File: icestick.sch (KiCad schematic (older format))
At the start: 2 parts, among them J1 Conn_01x10, J3 Conn_01x10

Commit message: Assigned footprints
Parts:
- J1, J3: footprint (none) -> Connector_PinHeader_2.54mm:PinHeader_1x10_P2.54mm_Vertical
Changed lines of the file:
@@
 F 0 "J1" H 2900 3700 50  0000 C CNN
 F 1 "Conn_01x10" H 2850 2500 50  0001 C CNN
-F 2 "" H 2900 3150 50  0001 C CNN
+F 2 "Connector_PinHeader_2.54mm:PinHeader_1x10_P2.54mm_Vertical" H 2900 3150 50  0001 C CNN
 F 3 "~" H 2900 3150 50  0001 C CNN
 	1    2900 3150
@@
 F 0 "J3" H 5720 3675 50  0000 C CNN
 F 1 "Conn_01x10" H 5720 3676 50  0001 C CNN
-F 2 "" H 5800 3150 50  0001 C CNN
+F 2 "Connector_PinHeader_2.54mm:PinHeader_1x10_P2.54mm_Vertical" H 5800 3150 50  0001 C CNN
 F 3 "~" H 5800 3150 50  0001 C CNN
 	1    5800 3150

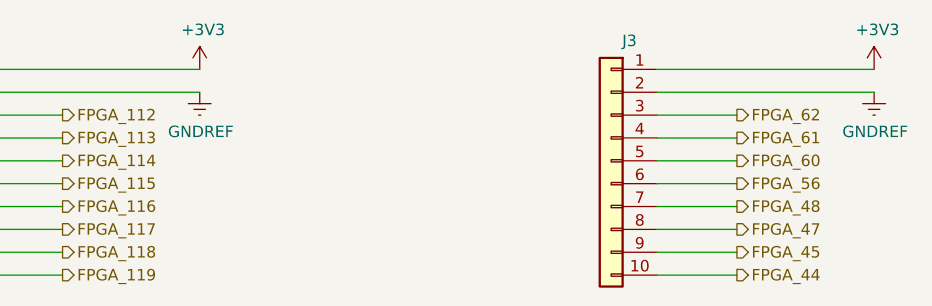
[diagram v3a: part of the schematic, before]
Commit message: Continued layouting
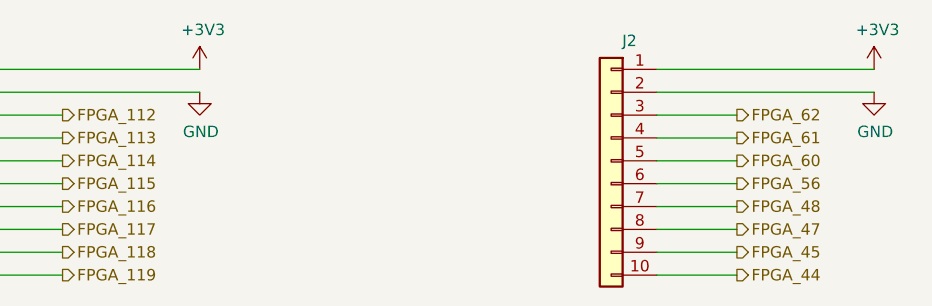
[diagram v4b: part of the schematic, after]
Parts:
- renumbered J3 to J2
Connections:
- net GNDREF renamed GND
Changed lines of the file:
@@
 $EndComp
 $Comp
-L power:+3V3 #PWR0101
+L power:+3V3 #PWR01
 U 1 1 5BCC5C29
 P 4000 2750
-F 0 "#PWR0101" H 4000 2600 50  0001 C CNN
+F 0 "#PWR01" H 4000 2600 50  0001 C CNN
 F 1 "+3V3" H 4015 2923 50  0000 C CNN
 F 2 "" H 4000 2750 50  0001 C CNN
@@
 Wire Wire Line
 	3100 2850 4000 2850
-$Comp
-L power:GNDREF #PWR0102
-U 1 1 5BCC6126
-P 4000 2850
-F 0 "#PWR0102" H 4000 2600 50  0001 C CNN
-F 1 "GNDREF" H 4005 2677 50  0000 C CNN
-F 2 "" H 4000 2850 50  0001 C CNN
-F 3 "" H 4000 2850 50  0001 C CNN
-	1    4000 2850
-	1    0    0    -1
-$EndComp
 Wire Wire Line
 	4000 2750 3100 2750
 $Comp
-L Connector_Generic:Conn_01x10 J3
+L Connector_Generic:Conn_01x10 J2
 U 1 1 5BCC6CE9
 P 5800 3150
-F 0 "J3" H 5720 3675 50  0000 C CNN
+F 0 "J2" H 5720 3675 50  0000 C CNN
 F 1 "Conn_01x10" H 5720 3676 50  0001 C CNN
 F 2 "Connector_PinHeader_2.54mm:PinHeader_1x10_P2.54mm_Vertical" H 5800 3150 50  0001 C CNN
@@
 $EndComp
 $Comp
-L power:+3V3 #PWR0103
+L power:+3V3 #PWR03
 U 1 1 5BCC6E8C
 P 6950 2750
-F 0 "#PWR0103" H 6950 2600 50  0001 C CNN
+F 0 "#PWR03" H 6950 2600 50  0001 C CNN
 F 1 "+3V3" H 6965 2923 50  0000 C CNN
 F 2 "" H 6950 2750 50  0001 C CNN
 F 3 "" H 6950 2750 50  0001 C CNN
 	1    6950 2750
-	1    0    0    -1
-$EndComp
-$Comp
-L power:GNDREF #PWR0104
-U 1 1 5BCC6E9B
-P 6950 2850
-F 0 "#PWR0104" H 6950 2600 50  0001 C CNN
-F 1 "GNDREF" H 6955 2677 50  0000 C CNN
-F 2 "" H 6950 2850 50  0001 C CNN
-F 3 "" H 6950 2850 50  0001 C CNN
-	1    6950 2850
 	1    0    0    -1
 $EndComp
@@
 Wire Wire Line
 	6000 3650 6350 3650
+$Comp
+L power:GND #PWR04
+U 1 1 5BCF7627
+P 6950 2850
+F 0 "#PWR04" H 6950 2600 50  0001 C CNN
+F 1 "GND" H 6955 2677 50  0000 C CNN
+F 2 "" H 6950 2850 50  0001 C CNN
+F 3 "" H 6950 2850 50  0001 C CNN
+	1    6950 2850
+	1    0    0    -1
+$EndComp
+$Comp
+L power:GND #PWR02
+U 1 1 5BCF767D
+P 4000 2850
+F 0 "#PWR02" H 4000 2600 50  0001 C CNN
+F 1 "GND" H 4005 2677 50  0000 C CNN
+F 2 "" H 4000 2850 50  0001 C CNN
+F 3 "" H 4000 2850 50  0001 C CNN
+	1    4000 2850
+	1    0    0    -1
+$EndComp
 $EndSCHEMATC

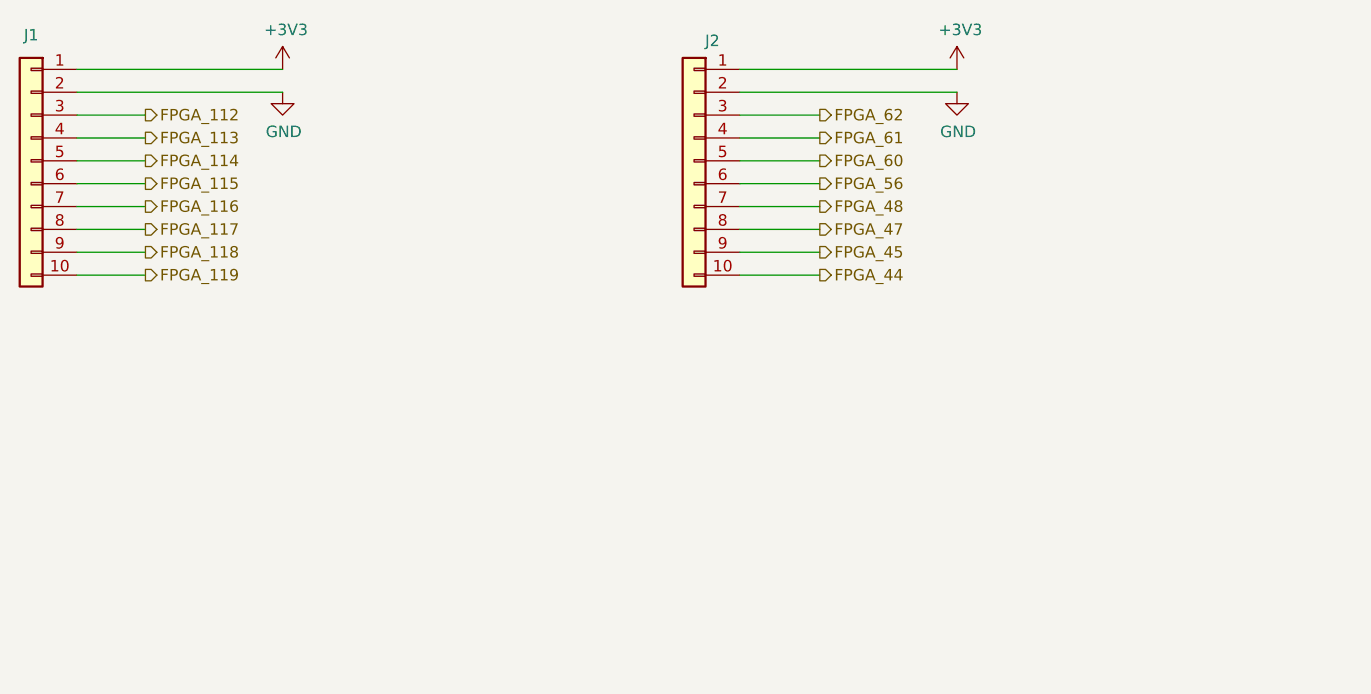
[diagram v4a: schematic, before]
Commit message: Began redesigning with Si8660
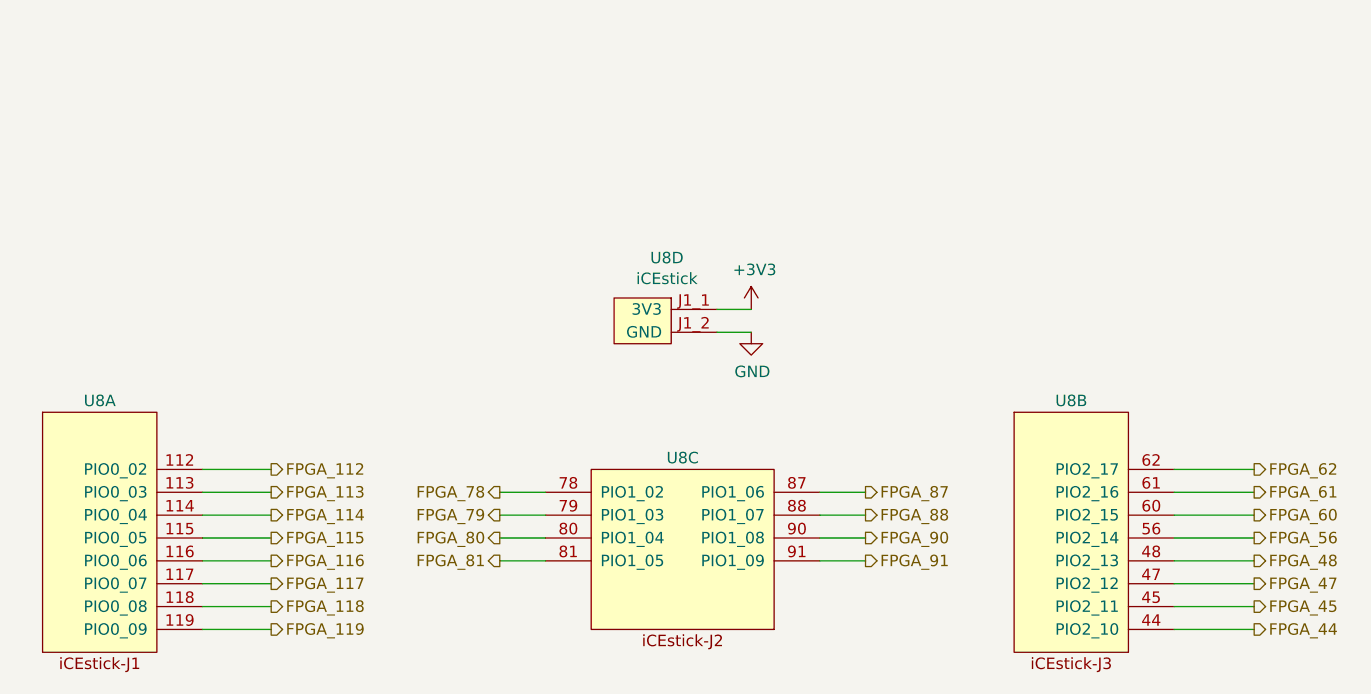
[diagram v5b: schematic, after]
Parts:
- removed J1, J2: Conn_01x10, Connector_PinHeader_2.54mm:PinHeader_1x10_P2.54mm_Vertical, symbol Connector_Generic:Conn_01x10
- added U8: iCEstick, Matthias:iCEstick, symbol Matthias:iCEstick
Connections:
- net +3V3: now also U8.J1_1 (3V3), U8.J2_12 (3V3), U8.J2_6 (3V3), U8.J3_1 (3V3)
- net FPGA_112: now also U8.112 (PIO0_02)
- net FPGA_113: now also U8.113 (PIO0_03)
- net FPGA_114: now also U8.114 (PIO0_04)
- net FPGA_115: now also U8.115 (PIO0_05)
- net FPGA_116: now also U8.116 (PIO0_06)
- net FPGA_117: now also U8.117 (PIO0_07)
- net FPGA_118: now also U8.118 (PIO0_08)
- net FPGA_119: now also U8.119 (PIO0_09)
- net FPGA_44: now also U8.44 (PIO2_10)
- net FPGA_45: now also U8.45 (PIO2_11)
- net FPGA_47: now also U8.47 (PIO2_12)
- net FPGA_48: now also U8.48 (PIO2_13)
- net FPGA_56: now also U8.56 (PIO2_14)
- net FPGA_60: now also U8.60 (PIO2_15)
- net FPGA_61: now also U8.61 (PIO2_16)
- net FPGA_62: now also U8.62 (PIO2_17)
- net GND: now also U8.J1_2 (GND), U8.J2_11 (GND), U8.J2_5 (GND), U8.J3_2 (GND)
- new net FPGA_78: U8.78 (PIO1_02)
- new net FPGA_79: U8.79 (PIO1_03)
- new net FPGA_80: U8.80 (PIO1_04)
- new net FPGA_81: U8.81 (PIO1_05)
- new net FPGA_87: U8.87 (PIO1_06)
- new net FPGA_88: U8.88 (PIO1_07)
- new net FPGA_90: U8.90 (PIO1_08)
- new net FPGA_91: U8.91 (PIO1_09)
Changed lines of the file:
@@
 $Descr A4 11693 8268
 encoding utf-8
-Sheet 2 11
+Sheet 11 11
 Title ""
 Date ""
@@
 Comment4 ""
 $EndDescr
-$Comp
-L Connector_Generic:Conn_01x10 J1
-U 1 1 5BCC5ADF
-P 2900 3150
-F 0 "J1" H 2900 3700 50  0000 C CNN
-F 1 "Conn_01x10" H 2850 2500 50  0001 C CNN
-F 2 "Connector_PinHeader_2.54mm:PinHeader_1x10_P2.54mm_Vertical" H 2900 3150 50  0001 C CNN
-F 3 "~" H 2900 3150 50  0001 C CNN
-	1    2900 3150
-	-1   0    0    -1
-$EndComp
-$Comp
-L power:+3V3 #PWR01
-U 1 1 5BCC5C29
-P 4000 2750
-F 0 "#PWR01" H 4000 2600 50  0001 C CNN
-F 1 "+3V3" H 4015 2923 50  0000 C CNN
-F 2 "" H 4000 2750 50  0001 C CNN
-F 3 "" H 4000 2750 50  0001 C CNN
-	1    4000 2750
-	1    0    0    -1
-$EndComp
-Text HLabel 3400 2950 2    50   Output ~ 0
+Text HLabel 3950 4500 2    50   Output ~ 0
 FPGA_112
-Text HLabel 3400 3050 2    50   Output ~ 0
+Text HLabel 3950 4600 2    50   Output ~ 0
 FPGA_113
-Text HLabel 3400 3150 2    50   Output ~ 0
+Text HLabel 3950 4700 2    50   Output ~ 0
 FPGA_114
-Text HLabel 3400 3250 2    50   Output ~ 0
+Text HLabel 3950 4800 2    50   Output ~ 0
 FPGA_115
-Text HLabel 3400 3350 2    50   Output ~ 0
+Text HLabel 3950 4900 2    50   Output ~ 0
 FPGA_116
-Text HLabel 3400 3450 2    50   Output ~ 0
+Text HLabel 3950 5000 2    50   Output ~ 0
 FPGA_117
-Text HLabel 3400 3550 2    50   Output ~ 0
+Text HLabel 3950 5100 2    50   Output ~ 0
 FPGA_118
-Text HLabel 3400 3650 2    50   Output ~ 0
+Text HLabel 3950 5200 2    50   Output ~ 0
 FPGA_119
 Wire Wire Line
-	3400 3650 3100 3650
+	3950 5200 3650 5200
 Wire Wire Line
-	3100 3550 3400 3550
+	3650 5100 3950 5100
 Wire Wire Line
-	3400 3450 3100 3450
+	3950 5000 3650 5000
 Wire Wire Line
-	3100 3350 3400 3350
+	3650 4900 3950 4900
 Wire Wire Line
-	3100 3250 3400 3250
+	3650 4800 3950 4800
 Wire Wire Line
-	3100 3150 3400 3150
+	3650 4700 3950 4700
 Wire Wire Line
-	3100 3050 3400 3050
+	3650 4600 3950 4600
 Wire Wire Line
-	3100 2950 3400 2950
-Wire Wire Line
-	3100 2850 4000 2850
-Wire Wire Line
-	4000 2750 3100 2750
+	3650 4500 3950 4500
 $Comp
-L Connector_Generic:Conn_01x10 J2
-U 1 1 5BCC6CE9
-P 5800 3150
-F 0 "J2" H 5720 3675 50  0000 C CNN
-F 1 "Conn_01x10" H 5720 3676 50  0001 C CNN
-F 2 "Connector_PinHeader_2.54mm:PinHeader_1x10_P2.54mm_Vertical" H 5800 3150 50  0001 C CNN
-F 3 "~" H 5800 3150 50  0001 C CNN
-	1    5800 3150
-	-1   0    0    -1
-$EndComp
-$Comp
-L power:+3V3 #PWR03
+L power:+3V3 #PWR056
 U 1 1 5BCC6E8C
-P 6950 2750
-F 0 "#PWR03" H 6950 2600 50  0001 C CNN
-F 1 "+3V3" H 6965 2923 50  0000 C CNN
-F 2 "" H 6950 2750 50  0001 C CNN
-F 3 "" H 6950 2750 50  0001 C CNN
-	1    6950 2750
+P 6050 3800
+F 0 "#PWR056" H 6050 3650 50  0001 C CNN
+F 1 "+3V3" H 6065 3973 50  0000 C CNN
+F 2 "" H 6050 3800 50  0001 C CNN
+F 3 "" H 6050 3800 50  0001 C CNN
+	1    6050 3800
 	1    0    0    -1
 $EndComp
 Wire Wire Line
-	6950 2850 6000 2850
+	6050 3900 5900 3900
 Wire Wire Line
-	6000 2750 6950 2750
-Text HLabel 6350 2950 2    50   Output ~ 0
+	5900 3800 6050 3800
+Text HLabel 8250 4500 2    50   Output ~ 0
 FPGA_62
-Text HLabel 6350 3050 2    50   Output ~ 0
+Text HLabel 8250 4600 2    50   Output ~ 0
 FPGA_61
-Text HLabel 6350 3150 2    50   Output ~ 0
+Text HLabel 8250 4700 2    50   Output ~ 0
 FPGA_60
-Text HLabel 6350 3250 2    50   Output ~ 0
+Text HLabel 8250 4800 2    50   Output ~ 0
 FPGA_56
-Text HLabel 6350 3350 2    50   Output ~ 0
+Text HLabel 8250 4900 2    50   Output ~ 0
 FPGA_48
-Text HLabel 6350 3450 2    50   Output ~ 0
+Text HLabel 8250 5000 2    50   Output ~ 0
 FPGA_47
-Text HLabel 6350 3550 2    50   Output ~ 0
+Text HLabel 8250 5100 2    50   Output ~ 0
 FPGA_45
-Text HLabel 6350 3650 2    50   Output ~ 0
+Text HLabel 8250 5200 2    50   Output ~ 0
 FPGA_44
 Wire Wire Line
-	6350 2950 6000 2950
+	8250 4500 7900 4500
 Wire Wire Line
-	6000 3050 6350 3050
+	7900 4600 8250 4600
 Wire Wire Line
-	6000 3150 6350 3150
+	7900 4700 8250 4700
 Wire Wire Line
-	6000 3250 6350 3250
+	7900 4800 8250 4800
 Wire Wire Line
-	6000 3350 6350 3350
+	7900 4900 8250 4900
 Wire Wire Line
-	6000 3450 6350 3450
+	7900 5000 8250 5000
 Wire Wire Line
-	6000 3550 6350 3550
+	7900 5100 8250 5100
 Wire Wire Line
-	6000 3650 6350 3650
+	7900 5200 8250 5200
 $Comp
-L power:GND #PWR04
+L power:GND #PWR057
 U 1 1 5BCF7627
-P 6950 2850
-F 0 "#PWR04" H 6950 2600 50  0001 C CNN
-F 1 "GND" H 6955 2677 50  0000 C CNN
-F 2 "" H 6950 2850 50  0001 C CNN
-F 3 "" H 6950 2850 50  0001 C CNN
-	1    6950 2850
+P 6050 3900
+F 0 "#PWR057" H 6050 3650 50  0001 C CNN
+F 1 "GND" H 6055 3727 50  0000 C CNN
+F 2 "" H 6050 3900 50  0001 C CNN
+F 3 "" H 6050 3900 50  0001 C CNN
+	1    6050 3900
 	1    0    0    -1
 $EndComp
 $Comp
-L power:GND #PWR02
-U 1 1 5BCF767D
-P 4000 2850
-F 0 "#PWR02" H 4000 2600 50  0001 C CNN
-F 1 "GND" H 4005 2677 50  0000 C CNN
-F 2 "" H 4000 2850 50  0001 C CNN
-F 3 "" H 4000 2850 50  0001 C CNN
-	1    4000 2850
+L Matthias:iCEstick U8
+U 1 1 5BE7665D
+P 3450 5300
+F 0 "U8" H 3200 6400 50  0000 C CNN
+F 1 "iCEstick" H 3306 6424 50  0001 C CNN
+F 2 "Matthias:iCEstick" H 2750 5650 50  0001 C CNN
+F 3 "" H 2750 5650 50  0001 C CNN
+	1    3450 5300
 	1    0    0    -1
 $EndComp
+$Comp
+L Matthias:iCEstick U8
+U 2 1 5BE76717
+P 7700 5300
+F 0 "U8" H 7450 6400 50  0000 C CNN
+F 1 "iCEstick" H 7556 6424 50  0001 C CNN
+F 2 "Matthias:iCEstick" H 7000 5650 50  0001 C CNN
+F 3 "" H 7000 5650 50  0001 C CNN
+	2    7700 5300
+	1    0    0    -1
+$EndComp
+$Comp
+L Matthias:iCEstick U8
+U 3 1 5BE7678E
+P 6000 5300
+F 0 "U8" H 5750 6150 50  0000 C CNN
+F 1 "iCEstick" H 5750 6174 50  0001 C CNN
+F 2 "Matthias:iCEstick" H 5300 5650 50  0001 C CNN
+F 3 "" H 5300 5650 50  0001 C CNN
+	3    6000 5300
+	1    0    0    -1
+$EndComp
+$Comp
+L Matthias:iCEstick U8
+U 4 1 5BE76801
+P 5700 4250
+F 0 "U8" H 5681 4925 50  0000 C CNN
+F 1 "iCEstick" H 5681 4834 50  0000 C CNN
+F 2 "Matthias:iCEstick" H 5000 4600 50  0001 C CNN
+F 3 "" H 5000 4600 50  0001 C CNN
+	4    5700 4250
+	1    0    0    -1
+$EndComp
+Wire Wire Line
+	6350 4600 6550 4600
+Wire Wire Line
+	6350 4700 6550 4700
+Wire Wire Line
+	6350 4800 6550 4800
+Wire Wire Line
+	6350 4900 6550 4900
+Wire Wire Line
+	5150 4600 4950 4600
+Wire Wire Line
+	5150 4700 4950 4700
+Wire Wire Line
+	5150 4800 4950 4800
+Wire Wire Line
+	5150 4900 4950 4900
+Text HLabel 4950 4600 0    50   Output ~ 0
+FPGA_78
+Text HLabel 4950 4700 0    50   Output ~ 0
+FPGA_79
+Text HLabel 4950 4800 0    50   Output ~ 0
+FPGA_80
+Text HLabel 4950 4900 0    50   Output ~ 0
+FPGA_81
+Text HLabel 6550 4600 2    50   Output ~ 0
+FPGA_87
+Text HLabel 6550 4700 2    50   Output ~ 0
+FPGA_88
+Text HLabel 6550 4800 2    50   Output ~ 0
+FPGA_90
+Text HLabel 6550 4900 2    50   Output ~ 0
+FPGA_91
 $EndSCHEMATC

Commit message: Finished layout with 4x Si8660
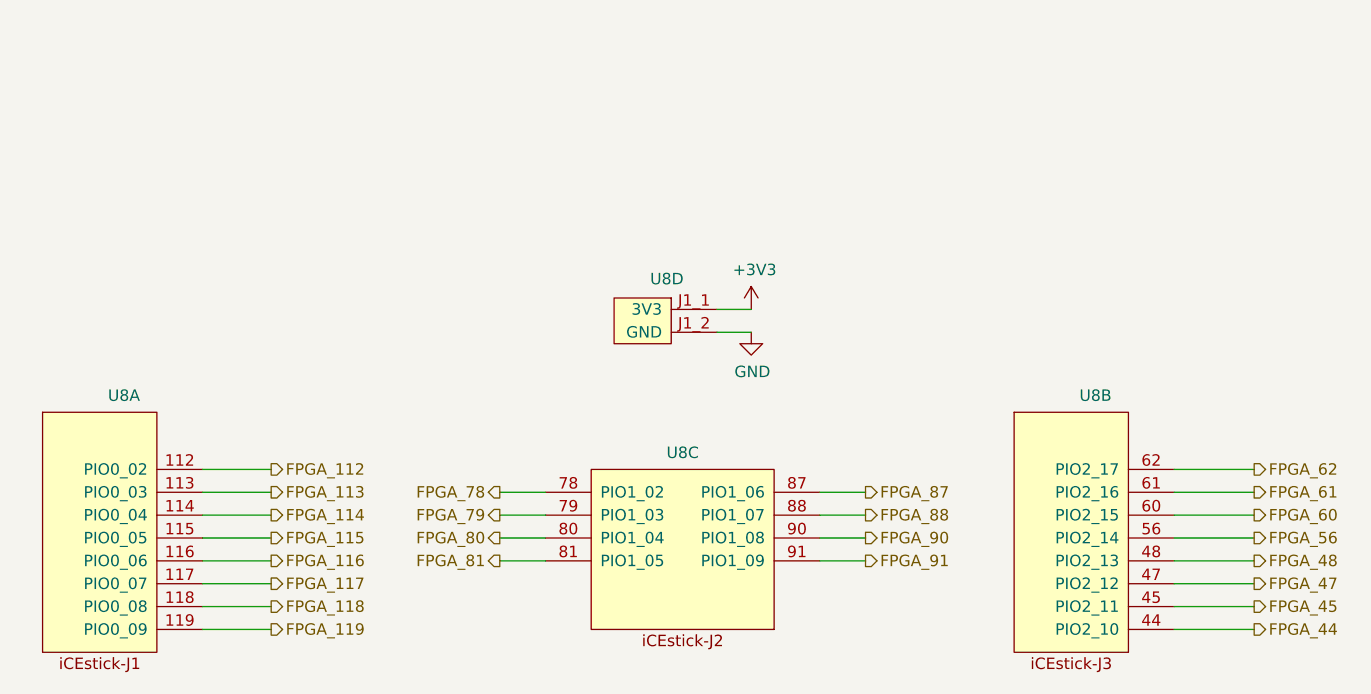
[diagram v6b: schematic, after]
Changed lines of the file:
@@
-	1    0    0    -1
-$EndComp
-$Comp
-L Matthias:iCEstick U8
-U 1 1 5BE7665D
-P 3450 5300
-F 0 "U8" H 3200 6400 50  0000 C CNN
-F 1 "iCEstick" H 3306 6424 50  0001 C CNN
-F 2 "Matthias:iCEstick" H 2750 5650 50  0001 C CNN
-F 3 "" H 2750 5650 50  0001 C CNN
-	1    3450 5300
-	1    0    0    -1
-$EndComp
-$Comp
-L Matthias:iCEstick U8
-U 2 1 5BE76717
-P 7700 5300
-F 0 "U8" H 7450 6400 50  0000 C CNN
-F 1 "iCEstick" H 7556 6424 50  0001 C CNN
-F 2 "Matthias:iCEstick" H 7000 5650 50  0001 C CNN
-F 3 "" H 7000 5650 50  0001 C CNN
-	2    7700 5300
-	1    0    0    -1
-$EndComp
-$Comp
-L Matthias:iCEstick U8
-U 3 1 5BE7678E
-P 6000 5300
-F 0 "U8" H 5750 6150 50  0000 C CNN
-F 1 "iCEstick" H 5750 6174 50  0001 C CNN
-F 2 "Matthias:iCEstick" H 5300 5650 50  0001 C CNN
-F 3 "" H 5300 5650 50  0001 C CNN
-	3    6000 5300
-	1    0    0    -1
-$EndComp
-$Comp
-L Matthias:iCEstick U8
-U 4 1 5BE76801
-P 5700 4250
-F 0 "U8" H 5681 4925 50  0000 C CNN
-F 1 "iCEstick" H 5681 4834 50  0000 C CNN
-F 2 "Matthias:iCEstick" H 5000 4600 50  0001 C CNN
-F 3 "" H 5000 4600 50  0001 C CNN
-	4    5700 4250
 	1    0    0    -1
 $EndComp
@@
 Text HLabel 6550 4900 2    50   Output ~ 0
 FPGA_91
+$Comp
+L Matthias:iCEstick U8
+U 1 1 5BF1DEB4
+P 3450 5300
+F 0 "U8" H 3306 6423 50  0000 C CNN
+F 1 "iCEstick" H 3250 5150 50  0001 C CNN
+F 2 "Matthias:iCEstick" H 2750 5650 50  0001 C CNN
+F 3 "" H 2750 5650 50  0001 C CNN
+	1    3450 5300
+	1    0    0    -1
+$EndComp
+$Comp
+L Matthias:iCEstick U8
+U 2 1 5BF1DF2E
+P 7700 5300
+F 0 "U8" H 7556 6423 50  0000 C CNN
+F 1 "iCEstick" H 7500 5150 50  0001 C CNN
+F 2 "Matthias:iCEstick" H 7000 5650 50  0001 C CNN
+F 3 "" H 7000 5650 50  0001 C CNN
+	2    7700 5300
+	1    0    0    -1
+$EndComp
+$Comp
+L Matthias:iCEstick U8
+U 3 1 5BF1E00D
+P 6000 5300
+F 0 "U8" H 5750 6173 50  0000 C CNN
+F 1 "iCEstick" H 5800 5150 50  0001 C CNN
+F 2 "Matthias:iCEstick" H 5300 5650 50  0001 C CNN
+F 3 "" H 5300 5650 50  0001 C CNN
+	3    6000 5300
+	1    0    0    -1
+$EndComp
+$Comp
+L Matthias:iCEstick U8
+U 4 1 5BF1E0A3
+P 5700 4250
+F 0 "U8" H 5681 4833 50  0000 C CNN
+F 1 "iCEstick" H 5500 4100 50  0001 C CNN
+F 2 "Matthias:iCEstick" H 5000 4600 50  0001 C CNN
+F 3 "" H 5000 4600 50  0001 C CNN
+	4    5700 4250
+	1    0    0    -1
+$EndComp
 $EndSCHEMATC
